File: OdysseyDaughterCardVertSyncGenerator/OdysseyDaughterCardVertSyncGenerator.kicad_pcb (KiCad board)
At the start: 2 copper layers, 29 x 46.6 mm, 13 parts, among them Q1 2N3904, Q2 2N3906, Q3 2N3904, X1 OdysseyDaughterCard

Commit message: OdysseyDaughterCardVertSyncGenerator: Open and close in KiCad 6, fix symbol library path
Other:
- net class Default removed

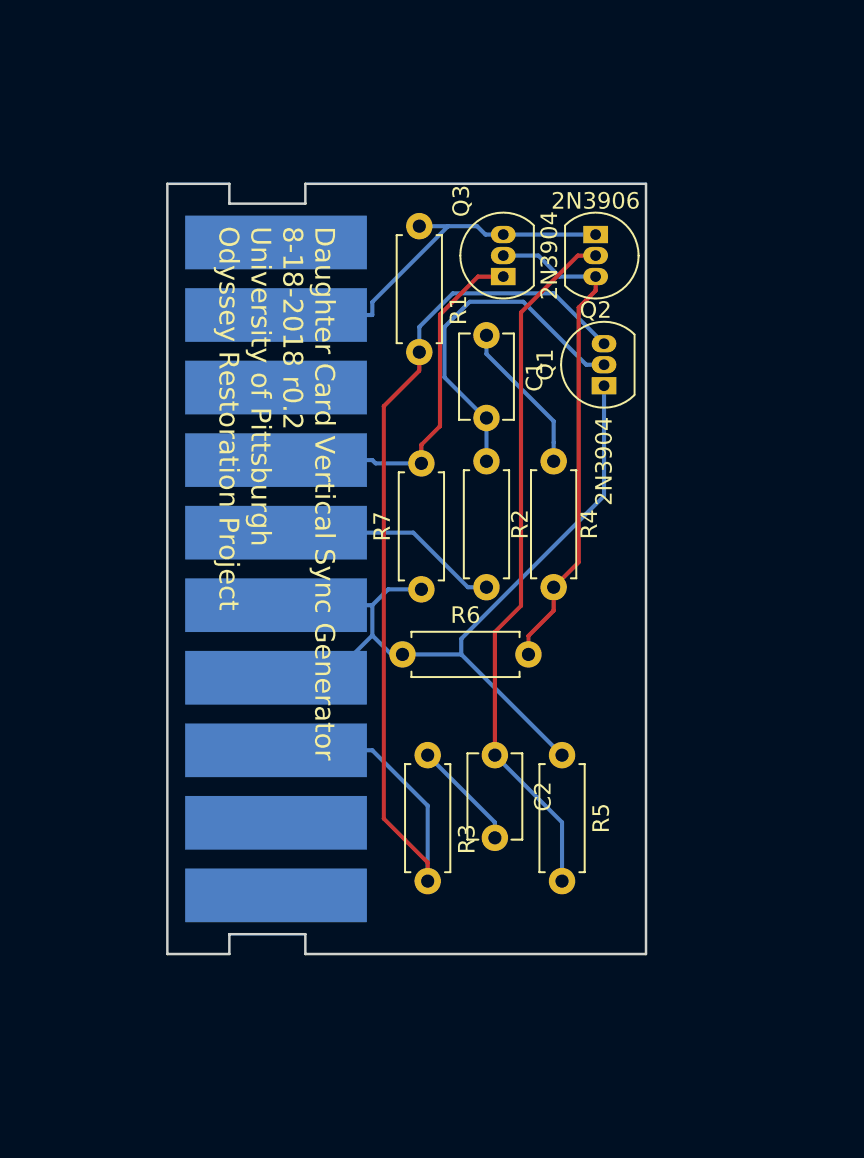
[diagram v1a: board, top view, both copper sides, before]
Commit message: OdysseyDaughterCardVertSyncGenerator wider transistor footprint, add logo, generate pdf, images, 3d models
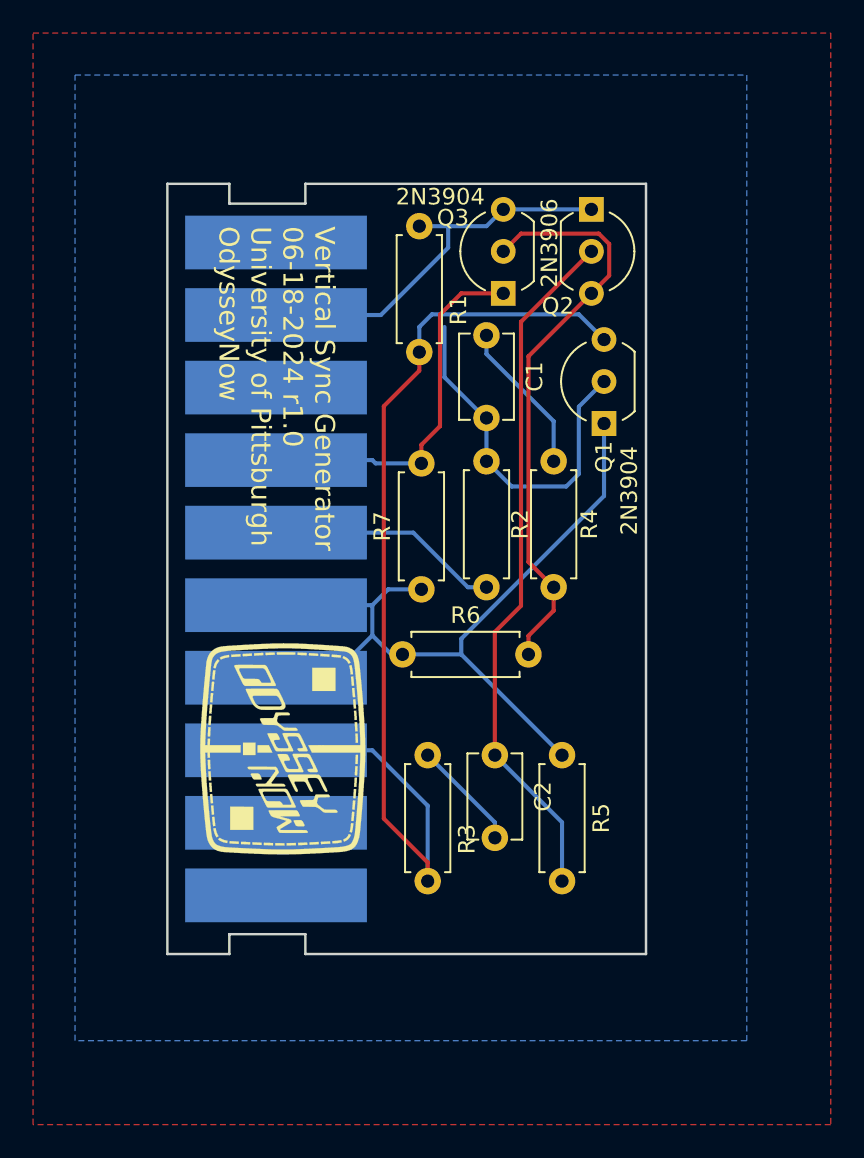
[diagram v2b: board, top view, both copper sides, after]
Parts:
- added X2: OdysseyNow_Logo, Odyssey_Daughter_Card:OdysseyNowLogo, F.Cu at (130.2, 111.6)
- Q1, Q2, Q3: footprint Package_TO_SOT_THT:TO-92_Inline -> Package_TO_SOT_THT:TO-92_Inline_Wide
- moved Q1 2.29 mm to (148.8, 92.2)
- moved Q2 1.55 mm to (148.1, 79.2)
- moved Q3 1.02 mm to (142.7, 84.3)
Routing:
- net Net-(Q2-C): track 30.7 -> 35.2 mm
- net GND: track 52.2 -> 49.9 mm
- net /Card3: track 63.9 -> 62.8 mm
- net Net-(Q1-B): track 21.1 -> 22.0 mm
- added copper zone on F.Cu, net /Card9
- added copper zone on B.Cu, net GND
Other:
- board text added: "Vertical Sync Generator 06-18-2024 r1.0 University of Pittsburgh OdysseyNow"
- board text removed: "Daughter Card Vertical Sync Generator 8-18-2018 r0.2 University of Pittsburgh Odyssey Restoration Project"
